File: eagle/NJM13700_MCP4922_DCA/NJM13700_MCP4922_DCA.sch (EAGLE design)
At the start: 38 parts, among them IC1 LM13600AN, IC2 MCP4922, IC3 TL072, IC4 TA480335, T1 2SA1015

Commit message: change parameters
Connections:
- net AGND: now also IC1A.+IN, IC1B.-IN; no longer IC1A.-IN, IC1B.+IN
- net N$10: now also IC3B.-IN; no longer IC3A.-IN
- net N$12: now also IC1B.AMP/BIAS; no longer IC1A.AMP/BIAS
- net N$14: now also IC1A.-IN, IC1A.BUFF/IN, IC1A.OUT; no longer IC1B.-IN, IC1B.BUFF/IN, IC1B.OUT
- net N$16: now also IC3A.-IN, IC3A.OUT; no longer IC3B.-IN, IC3B.OUT
- net N$4: now also IC1B.+IN; no longer IC1A.+IN
- net N$5: now also IC1B.BUFF/IN, IC1B.OUT; no longer IC1A.BUFF/IN, IC1A.OUT
- net N$6: now also IC1B.BUFF/OUT; no longer IC1A.BUFF/OUT
- net N$9: now also IC3B.OUT; no longer IC3A.OUT
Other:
- moved on the sheet: IC1A, IC1B, IC3A, IC3B
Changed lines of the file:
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@@
 <instance part="R3" gate="G$1" x="83.82" y="91.44" rot="R90"/>
 <instance part="AGND3" gate="VR1" x="83.82" y="81.28"/>
-<instance part="IC1" gate="A" x="114.3" y="101.6"/>
+<instance part="IC1" gate="B" x="114.3" y="101.6"/>
 <instance part="IC1" gate="P" x="231.14" y="93.98"/>
-<instance part="IC1" gate="B" x="200.66" y="93.98"/>
+<instance part="IC1" gate="A" x="200.66" y="93.98"/>
 <instance part="AGND4" gate="VR1" x="93.98" y="104.14" rot="R270"/>
 <instance part="R4" gate="G$1" x="134.62" y="88.9" rot="R90"/>
@@
 <instance part="C3" gate="G$1" x="101.6" y="40.64"/>
 <instance part="AGND10" gate="VR1" x="101.6" y="27.94"/>
-<instance part="IC3" gate="A" x="127" y="55.88"/>
+<instance part="IC3" gate="B" x="127" y="55.88"/>
 <instance part="AGND11" gate="VR1" x="114.3" y="58.42" rot="R270"/>
 <instance part="R7" gate="G$1" x="109.22" y="53.34" rot="R180"/>
@@
 </instance>
 <instance part="R9" gate="G$1" x="154.94" y="88.9" rot="R90"/>
-<instance part="IC3" gate="B" x="200.66" y="60.96"/>
+<instance part="IC3" gate="A" x="200.66" y="60.96"/>
 <instance part="IC3" gate="P" x="231.14" y="58.42"/>
 <instance part="AGND12" gate="VR1" x="185.42" y="45.72"/>
@@
 <segment>
 <pinref part="AGND4" gate="VR1" pin="AGND"/>
-<pinref part="IC1" gate="A" pin="-IN"/>
+<pinref part="IC1" gate="B" pin="-IN"/>
 <wire x1="96.52" y1="104.14" x2="99.06" y2="104.14" width="0.1524" layer="91"/>
 </segment>
@@
 <segment>
 <pinref part="AGND11" gate="VR1" pin="AGND"/>
-<pinref part="IC3" gate="A" pin="+IN"/>
+<pinref part="IC3" gate="B" pin="+IN"/>
 <wire x1="116.84" y1="58.42" x2="119.38" y2="58.42" width="0.1524" layer="91"/>
 </segment>
@@
 </segment>
 <segment>
-<pinref part="IC3" gate="B" pin="+IN"/>
+<pinref part="IC3" gate="A" pin="+IN"/>
 <pinref part="AGND12" gate="VR1" pin="AGND"/>
 <wire x1="193.04" y1="63.5" x2="185.42" y2="63.5" width="0.1524" layer="91"/>
@@
 </segment>
 <segment>
-<pinref part="IC1" gate="B" pin="+IN"/>
+<pinref part="IC1" gate="A" pin="+IN"/>
 <wire x1="185.42" y1="91.44" x2="182.88" y2="91.44" width="0.1524" layer="91"/>
 <pinref part="AGND13" gate="VR1" pin="AGND"/>
@@
 <pinref part="C1" gate="G$1" pin="-"/>
 <wire x1="83.82" y1="99.06" x2="81.28" y2="99.06" width="0.1524" layer="91"/>
-<pinref part="IC1" gate="A" pin="+IN"/>
+<pinref part="IC1" gate="B" pin="+IN"/>
 <wire x1="83.82" y1="99.06" x2="99.06" y2="99.06" width="0.1524" layer="91"/>
 <junction x="83.82" y="99.06"/>
@@
 <net name="N$5" class="0">
 <segment>
-<pinref part="IC1" gate="A" pin="OUT"/>
+<pinref part="IC1" gate="B" pin="OUT"/>
 <wire x1="132.08" y1="101.6" x2="134.62" y2="101.6" width="0.1524" layer="91"/>
 <wire x1="134.62" y1="101.6" x2="134.62" y2="96.52" width="0.1524" layer="91"/>
-<pinref part="IC1" gate="A" pin="BUFF/IN"/>
+<pinref part="IC1" gate="B" pin="BUFF/IN"/>
 <wire x1="134.62" y1="96.52" x2="132.08" y2="96.52" width="0.1524" layer="91"/>
 <pinref part="R4" gate="G$1" pin="2"/>
@@
 <net name="N$6" class="0">
 <segment>
-<pinref part="IC1" gate="A" pin="BUFF/OUT"/>
+<pinref part="IC1" gate="B" pin="BUFF/OUT"/>
 <wire x1="132.08" y1="106.68" x2="142.24" y2="106.68" width="0.1524" layer="91"/>
 <pinref part="R5" gate="G$1" pin="2"/>
@@
 <segment>
 <pinref part="R7" gate="G$1" pin="1"/>
-<pinref part="IC3" gate="A" pin="-IN"/>
+<pinref part="IC3" gate="B" pin="-IN"/>
 <wire x1="114.3" y1="53.34" x2="116.84" y2="53.34" width="0.1524" layer="91"/>
 <wire x1="116.84" y1="53.34" x2="119.38" y2="53.34" width="0.1524" layer="91"/>
@@
 <net name="N$9" class="0">
 <segment>
-<pinref part="IC3" gate="A" pin="OUT"/>
+<pinref part="IC3" gate="B" pin="OUT"/>
 <pinref part="T1" gate="G$1" pin="B"/>
 <wire x1="134.62" y1="55.88" x2="142.24" y2="55.88" width="0.1524" layer="91"/>
@@
 <net name="N$12" class="0">
 <segment>
-<pinref part="IC1" gate="A" pin="AMP/BIAS"/>
+<pinref part="IC1" gate="B" pin="AMP/BIAS"/>
 <wire x1="99.06" y1="93.98" x2="96.52" y2="93.98" width="0.1524" layer="91"/>
 <wire x1="96.52" y1="93.98" x2="96.52" y2="68.58" width="0.1524" layer="91"/>
@@
 <net name="N$16" class="0">
 <segment>
-<pinref part="IC3" gate="B" pin="-IN"/>
+<pinref part="IC3" gate="A" pin="-IN"/>
 <wire x1="193.04" y1="58.42" x2="190.5" y2="58.42" width="0.1524" layer="91"/>
 <wire x1="190.5" y1="58.42" x2="190.5" y2="50.8" width="0.1524" layer="91"/>
 <wire x1="190.5" y1="50.8" x2="210.82" y2="50.8" width="0.1524" layer="91"/>
 <wire x1="210.82" y1="50.8" x2="210.82" y2="60.96" width="0.1524" layer="91"/>
-<pinref part="IC3" gate="B" pin="OUT"/>
+<pinref part="IC3" gate="A" pin="OUT"/>
 <wire x1="210.82" y1="60.96" x2="208.28" y2="60.96" width="0.1524" layer="91"/>
 </segment>
@@
 <net name="N$14" class="0">
 <segment>
-<pinref part="IC1" gate="B" pin="-IN"/>
+<pinref part="IC1" gate="A" pin="-IN"/>
 <wire x1="185.42" y1="96.52" x2="182.88" y2="96.52" width="0.1524" layer="91"/>
 <wire x1="182.88" y1="96.52" x2="182.88" y2="109.22" width="0.1524" layer="91"/>
 <wire x1="182.88" y1="109.22" x2="223.52" y2="109.22" width="0.1524" layer="91"/>
 <wire x1="223.52" y1="109.22" x2="223.52" y2="93.98" width="0.1524" layer="91"/>
-<pinref part="IC1" gate="B" pin="OUT"/>
+<pinref part="IC1" gate="A" pin="OUT"/>
 <wire x1="223.52" y1="93.98" x2="218.44" y2="93.98" width="0.1524" layer="91"/>
-<pinref part="IC1" gate="B" pin="BUFF/IN"/>
+<pinref part="IC1" gate="A" pin="BUFF/IN"/>
 <wire x1="218.44" y1="88.9" x2="223.52" y2="88.9" width="0.1524" layer="91"/>
 <wire x1="223.52" y1="88.9" x2="223.52" y2="93.98" width="0.1524" layer="91"/>

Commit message: Add: Board design
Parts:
- added RCA1, RCA2: ATD_RCA_JACK-DIP, mylib2:ATD_RCA_JACK-DIP
- C10, C12, C8: device rcl:CPOL-EUE2.5-6 -> rcl:CPOL-EUE5-8.5
- C3: device rcl:C-EU050-025X075 -> rcl:C-EU050-024X044
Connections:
- net AGND: now also IC1A.-IN, IC1B.+IN, RCA1.S, RCA2.S; no longer IC1A.+IN, IC1B.-IN
- net N$1: now also RCA1.T
- net N$12: now also IC1A.AMP/BIAS; no longer IC1B.AMP/BIAS
- net N$14: now also IC1B.-IN, IC1B.BUFF/IN, IC1B.OUT; no longer IC1A.-IN, IC1A.BUFF/IN, IC1A.OUT
- net N$17: now also RCA2.T
- net N$4: now also IC1A.+IN; no longer IC1B.+IN
- net N$5: now also IC1A.BUFF/IN, IC1A.OUT; no longer IC1B.BUFF/IN, IC1B.OUT
- net N$6: now also IC1A.BUFF/OUT; no longer IC1B.BUFF/OUT
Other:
- moved on the sheet: C1, C10, C11, C12, C13, C2, C3, C4, C5, C6, C7, C8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

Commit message: updated schematic & board designe
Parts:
- added LED1, LED2: Green, led:LED3MM
- added R10, R11: 1k, rcl:R-EU_0207/7
- C1: device rcl:CPOL-EUE2.5-6 -> rcl:CPOL-EUE5-6
- IC4: value TA480335 -> TA48M033F
- JP4: value PIN -> (none); device pinhead:PINHD-1X3 -> pinhead:PINHD-1X4
- R4: value 33k -> 27k
- TP1: value TPB1,27 -> TPPAD1-13; device testpad:TPB1,27 -> testpad:TPPAD1-13
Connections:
- new net N$15: LED2.A, R11.1
- new net N$18: LED1.A, R10.1
- net +5V: now also R10.2
- net -5V: now also JP4.4, LED2.C; no longer JP4.3
- net AGND: now also JP4.3, LED1.C, R11.2
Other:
- moved on the sheet: C10, C11, C12, C8, C9, D1, IC4, JP7, JP8, JP9, RCA1, RCA2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

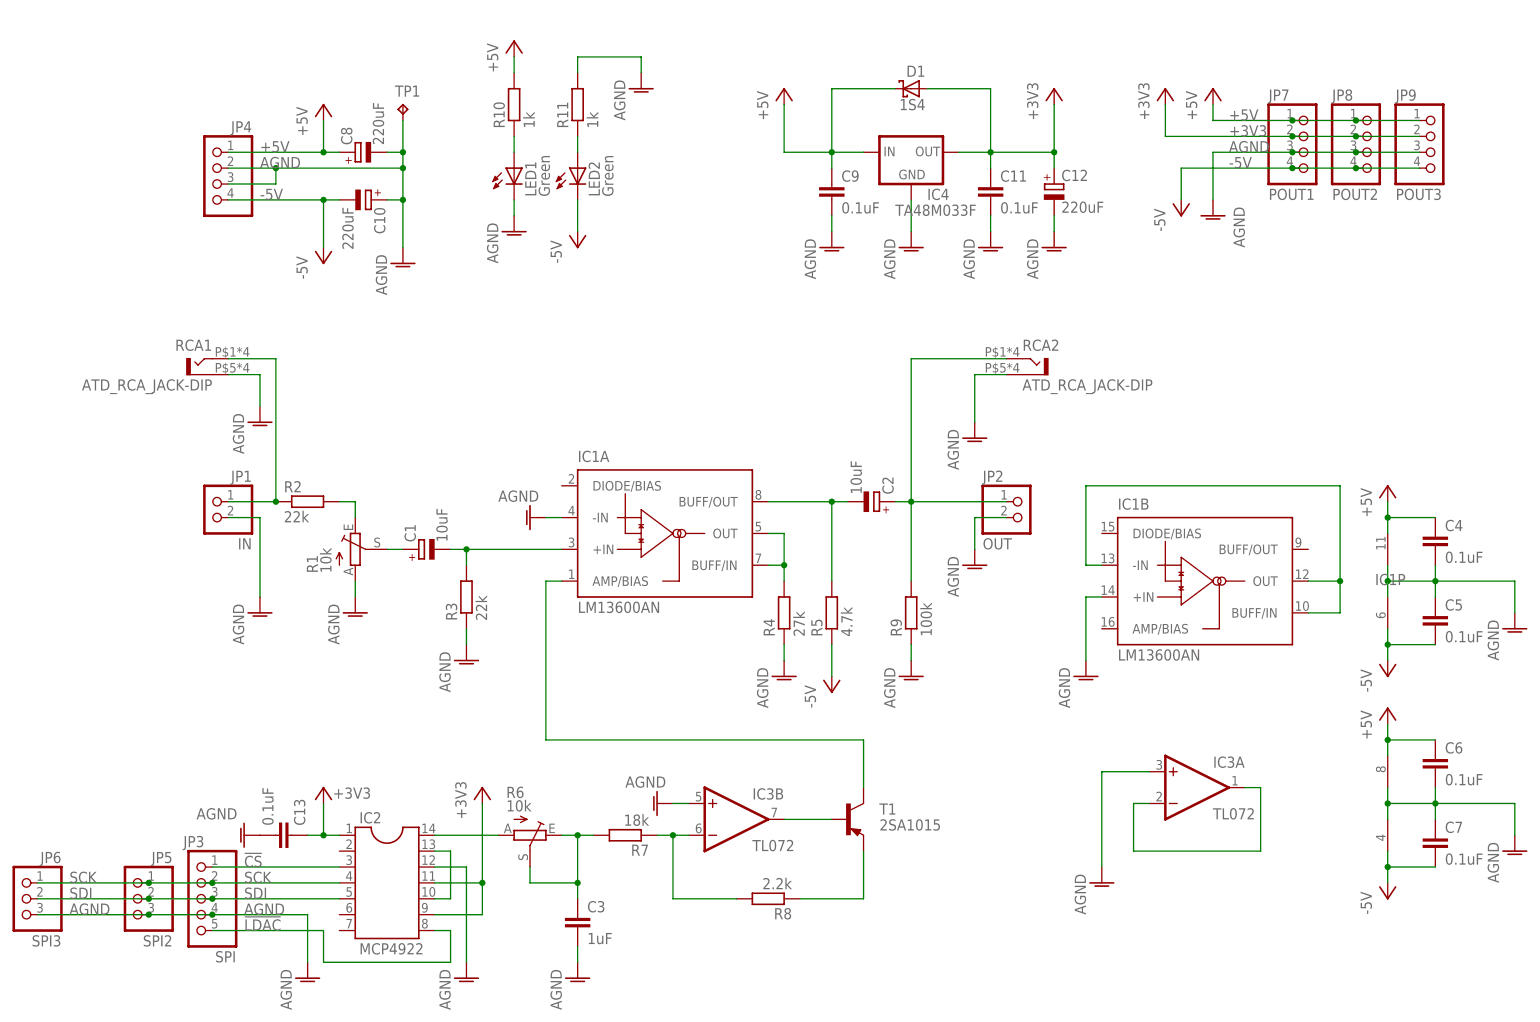
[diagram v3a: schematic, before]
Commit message: IC1、IC2の電源ラインのGNDへの接続を消去
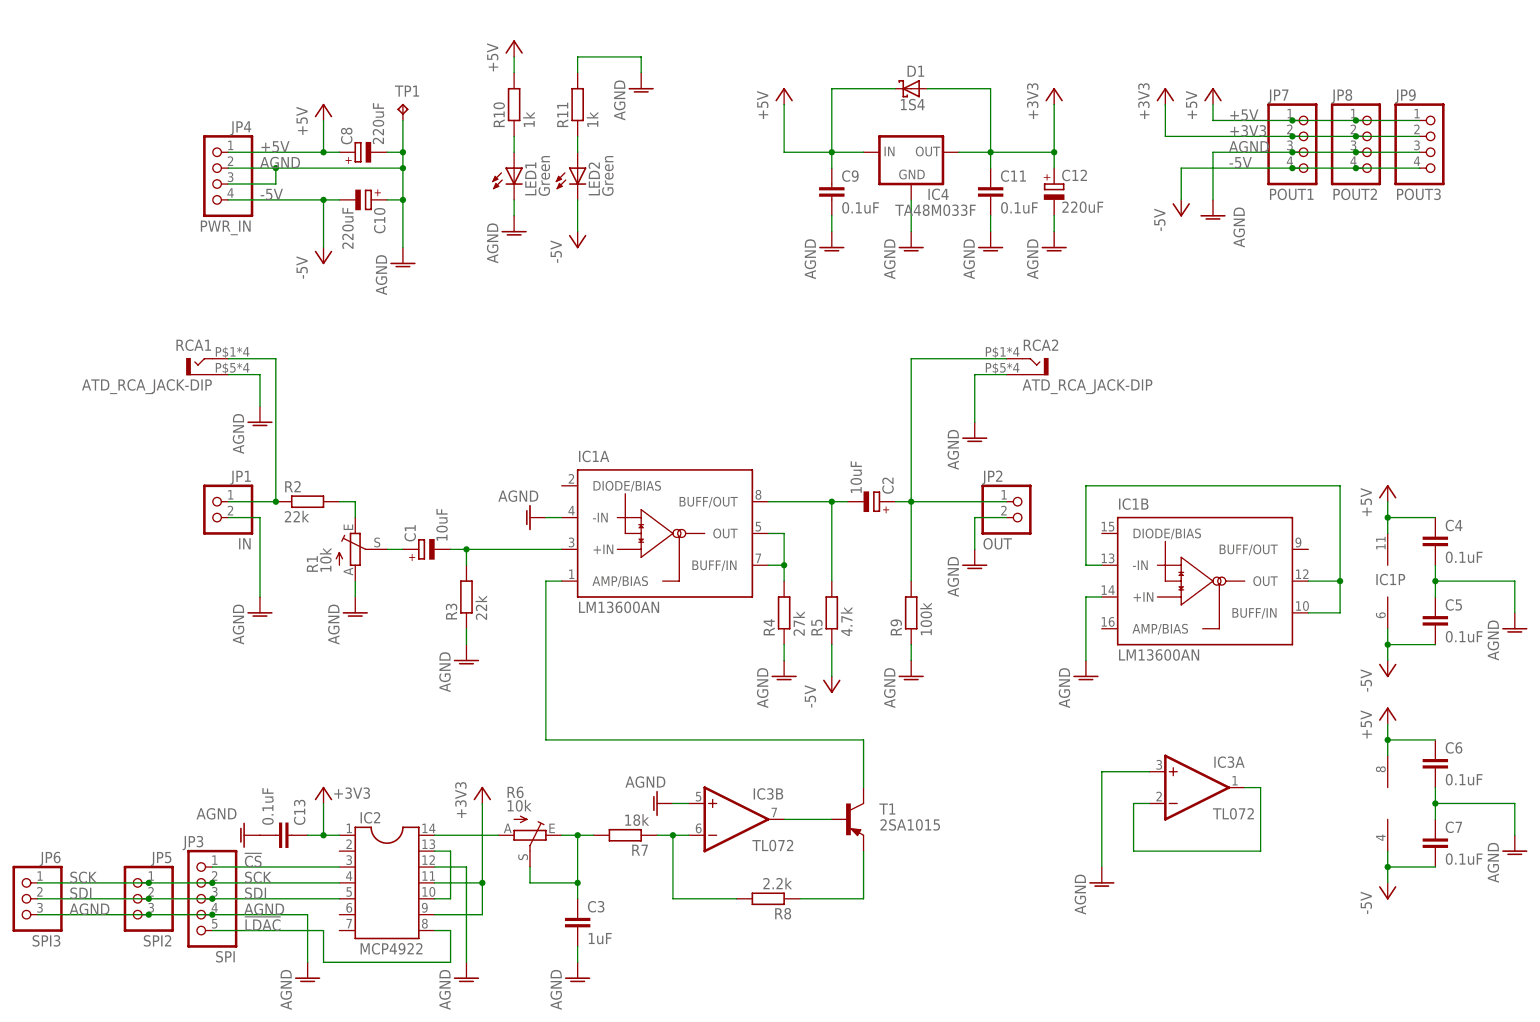
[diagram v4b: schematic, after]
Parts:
- JP4: value (none) -> PWR_IN
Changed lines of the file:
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@@
 <setting verticaltext="up"/>
 </settings>
-<grid distance="0.1" unitdist="inch" unit="inch" style="lines" multiple="1" display="yes" altdistance="0.01" altunitdist="inch" altunit="inch"/>
+<grid distance="0.1" unitdist="inch" unit="inch" style="lines" multiple="1" display="no" altdistance="0.01" altunitdist="inch" altunit="inch"/>
 <layers>
 <layer number="1" name="Top" color="4" fill="1" visible="no" active="no"/>
@@
 <part name="RCA1" library="mylib2" deviceset="ATD_RCA_JACK-DIP" device=""/>
 <part name="RCA2" library="mylib2" deviceset="ATD_RCA_JACK-DIP" device=""/>
-<part name="JP4" library="pinhead" deviceset="PINHD-1X4" device=""/>
+<part name="JP4" library="pinhead" deviceset="PINHD-1X4" device="" value="PWR_IN"/>
 <part name="LED1" library="led" deviceset="LED" device="3MM" value="Green"/>
 <part name="LED2" library="led" deviceset="LED" device="3MM" value="Green"/>
@@
 </segment>
 <segment>
-<wire x1="231.14" y1="78.74" x2="231.14" y2="81.28" width="0.1524" layer="91"/>
-<wire x1="231.14" y1="81.28" x2="231.14" y2="83.82" width="0.1524" layer="91"/>
-<wire x1="231.14" y1="81.28" x2="238.76" y2="81.28" width="0.1524" layer="91"/>
-<junction x="231.14" y="81.28"/>
 <pinref part="C5" gate="G$1" pin="1"/>
 <wire x1="238.76" y1="81.28" x2="238.76" y2="78.74" width="0.1524" layer="91"/>
@@
 </segment>
 <segment>
-<wire x1="231.14" y1="48.26" x2="231.14" y2="45.72" width="0.1524" layer="91"/>
-<wire x1="231.14" y1="45.72" x2="231.14" y2="43.18" width="0.1524" layer="91"/>
-<wire x1="231.14" y1="45.72" x2="238.76" y2="45.72" width="0.1524" layer="91"/>
-<junction x="231.14" y="45.72"/>
 <pinref part="C6" gate="G$1" pin="2"/>
 <wire x1="238.76" y1="45.72" x2="238.76" y2="48.26" width="0.1524" layer="91"/>
